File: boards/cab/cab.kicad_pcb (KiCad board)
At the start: 2 copper layers, 71.3 x 71.3 mm, 44 parts, among them J1 Conn_01x08_Female, J2 Conn_01x08_Female, J3 Conn_01x08_Female, J4 Conn_01x08_Female, Q1 SI2308A, Q2 S8550, Q3 BC817-40,215, Q4 S8550, Q5 BC817-40,215, Q6 S8550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

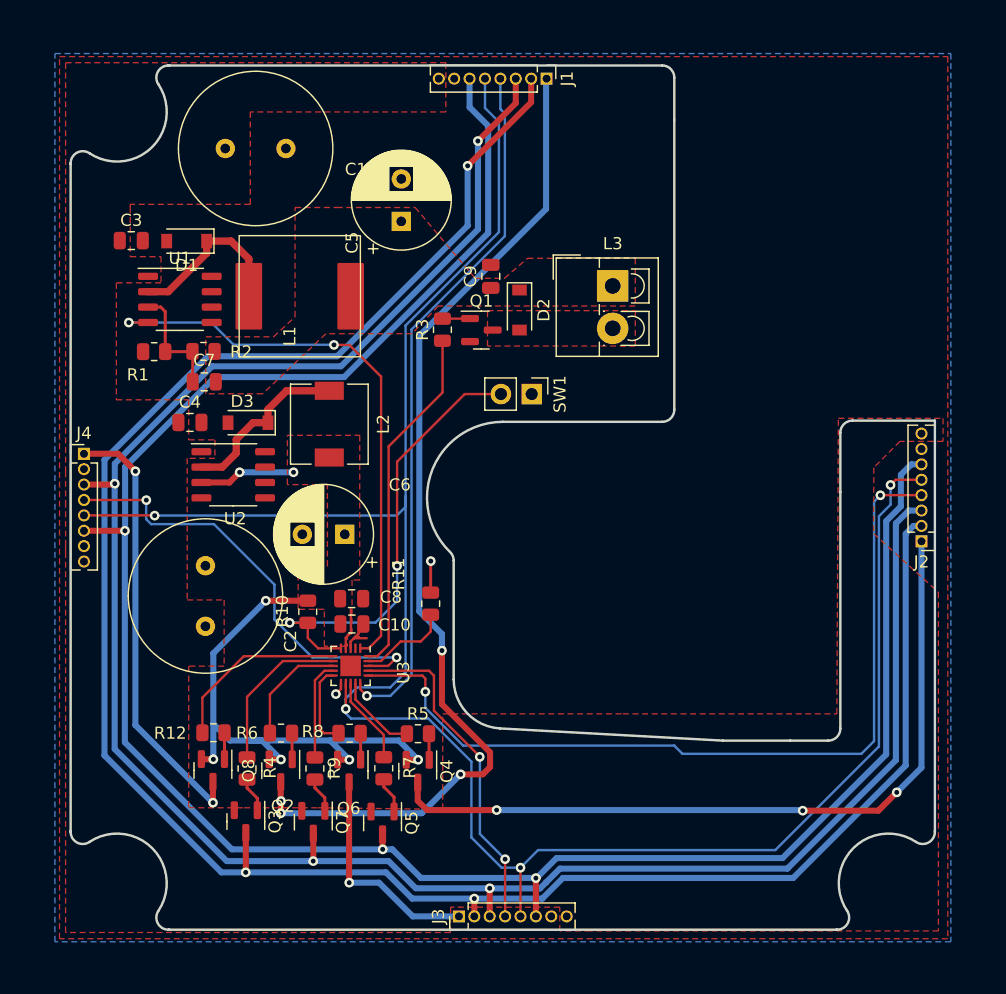
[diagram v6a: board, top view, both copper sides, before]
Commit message: Convert to 4 layer
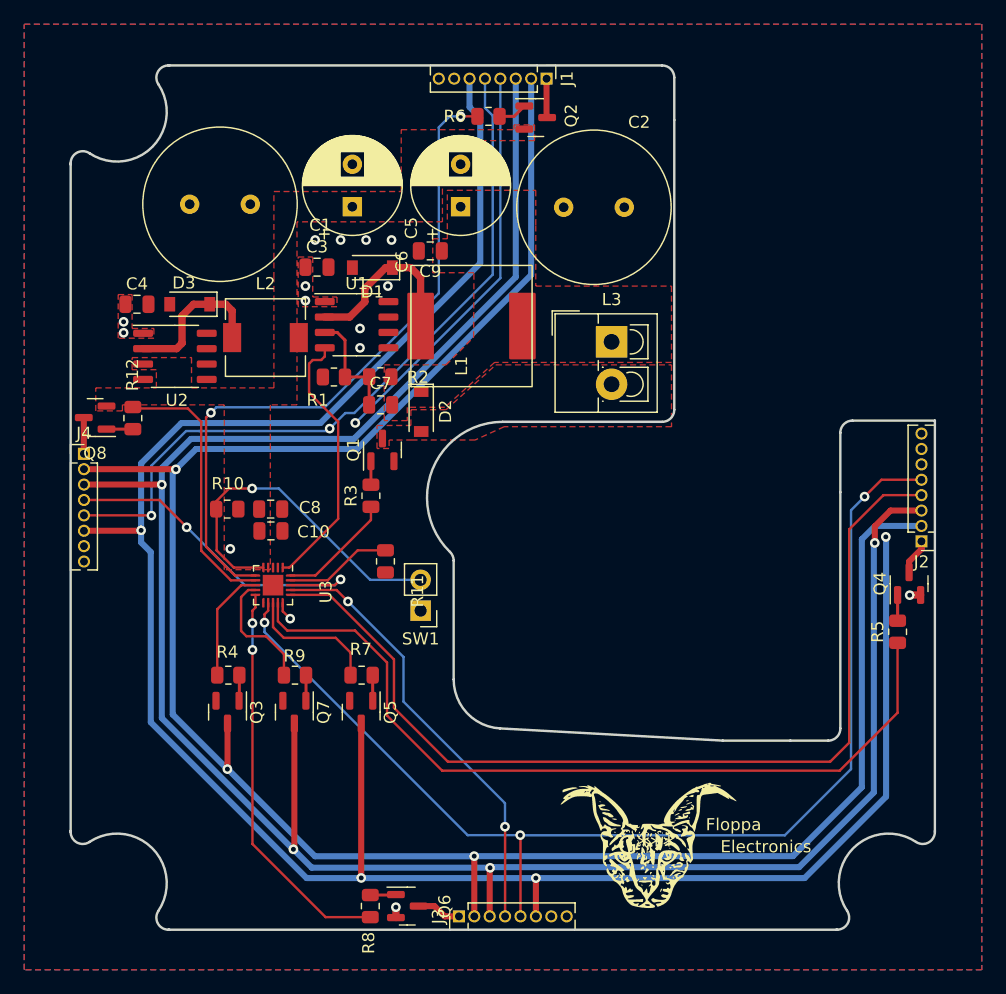
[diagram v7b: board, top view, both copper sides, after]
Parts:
- added G***: LOGO, LOGO, F.Cu at (106.3, 107.7)
- moved Q2 57.8 mm to (97.2, 47.7), turned to 0 degrees
- moved R6 53.7 mm to (93.3, 47.6)
- moved C2 48.9 mm to (104.5, 55.1), turned to 180 degrees
- moved Q4 43.4 mm to (128.0, 86.2), turned to 90 degrees
- moved R5 40.5 mm to (127.0, 90.1), turned to 90 degrees
- moved Q8 30.7 mm to (60.9, 72.5), turned to 180 degrees
- moved C6 27.0 mm to (82.1, 55.1), turned to 90 degrees
- moved R12 26.8 mm to (64.0, 72.5), turned to -90 degrees
- moved SW1 20.1 mm to (87.7, 88.4), turned to 180 degrees
- moved C3 15.5 mm to (79.2, 60.0)
- moved D1 15.5 mm to (83.7, 60.1)
- moved R1 15.0 mm to (80.5, 69.1)
- moved R3 14.9 mm to (83.6, 78.9)
- moved R2 14.7 mm to (84.4, 69.1)
- moved U1 14.7 mm to (82.4, 64.8)
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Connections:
- U3 pad 6: LED3_PWM -> LED0_PWM
- U3 pad 7: R_PWM -> LED3_PWM
- U3 pad 8: LED0_PWM -> R_PWM
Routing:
- net LED0: track 85.0 -> 3.23 mm, vias 4 -> 0
- net LED1_PWM: track 6.74 -> 68.1 mm
- net LED1: track 63.5 -> 2.98 mm, vias 3 -> 0
- net LED0_PWM: track 9.38 -> 56.4 mm, vias 0 -> 2
- net 5V: track 57.3 -> 94.8 mm, vias 7 -> 3
- net LED3: track 36.6 -> 2.99 mm, vias 2 -> 0
- net LED2_PWM: track 6.85 -> 32.9 mm, vias 0 -> 2
- net 24V_EN: track 47.8 -> 22.3 mm, vias 2 -> 0
- net SOL_EN: track 29.0 -> 9.61 mm
- net LED2: track 18.5 -> 3.67 mm, vias 1 -> 0
- net G: track 179.1 -> 191.1 mm, vias 3 -> 4
- net SEL1: track 70.1 -> 79.5 mm, vias 2 -> 0
- net CAB_STATE: track 37.8 -> 28.9 mm, vias 2 -> 1
- net SEL2: track 27.9 -> 36.5 mm
- net B: track 178.4 -> 186.5 mm
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- added copper zone on In2.Cu, net GND
- added copper zone on In1.Cu, net VBUS
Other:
- copper layers 2 -> 4
- board text added: "Electronics"
- board text added: "Floppa"

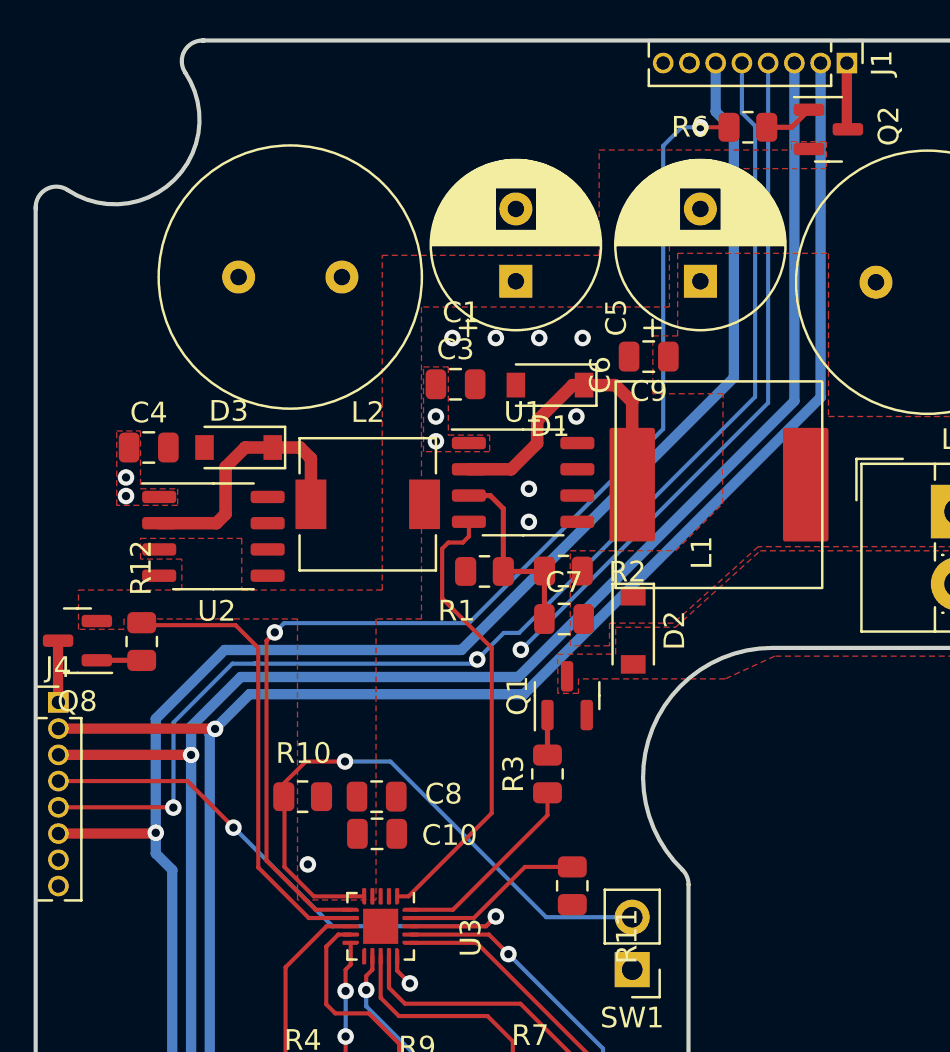
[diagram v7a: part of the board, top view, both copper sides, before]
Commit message: Added vias
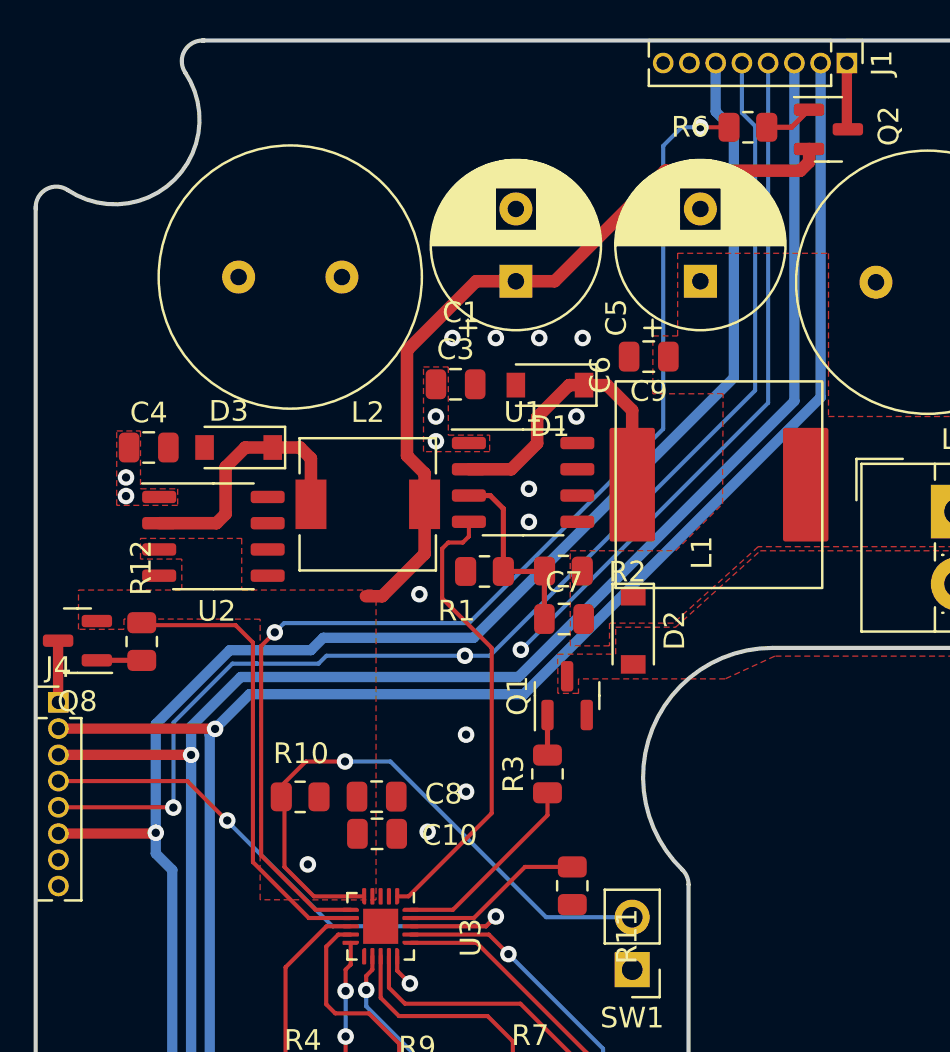
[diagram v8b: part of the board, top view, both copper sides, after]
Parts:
- moved R10 0.12 mm to (71.6, 80.0)
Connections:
- U1 pad 6: (no net) -> GND
- U1 pad 7: (no net) -> GND
- U1 pad 8: (no net) -> GND
- U2 pad 6: (no net) -> GND
- U2 pad 7: (no net) -> GND
- U2 pad 8: (no net) -> GND
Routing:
- net 5V: track 94.8 -> 132.6 mm
- net GDA: track 174.7 -> 174.0 mm
- net GND: vias 7 -> 11
